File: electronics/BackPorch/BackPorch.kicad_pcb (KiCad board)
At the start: 2 copper layers, 58.7 x 41.7 mm, 15 parts, among them J1 RJ45, J2 RJ45, J3 2601-1102, J4 2601-1104, J5 2601-1104, J6 2601-1104

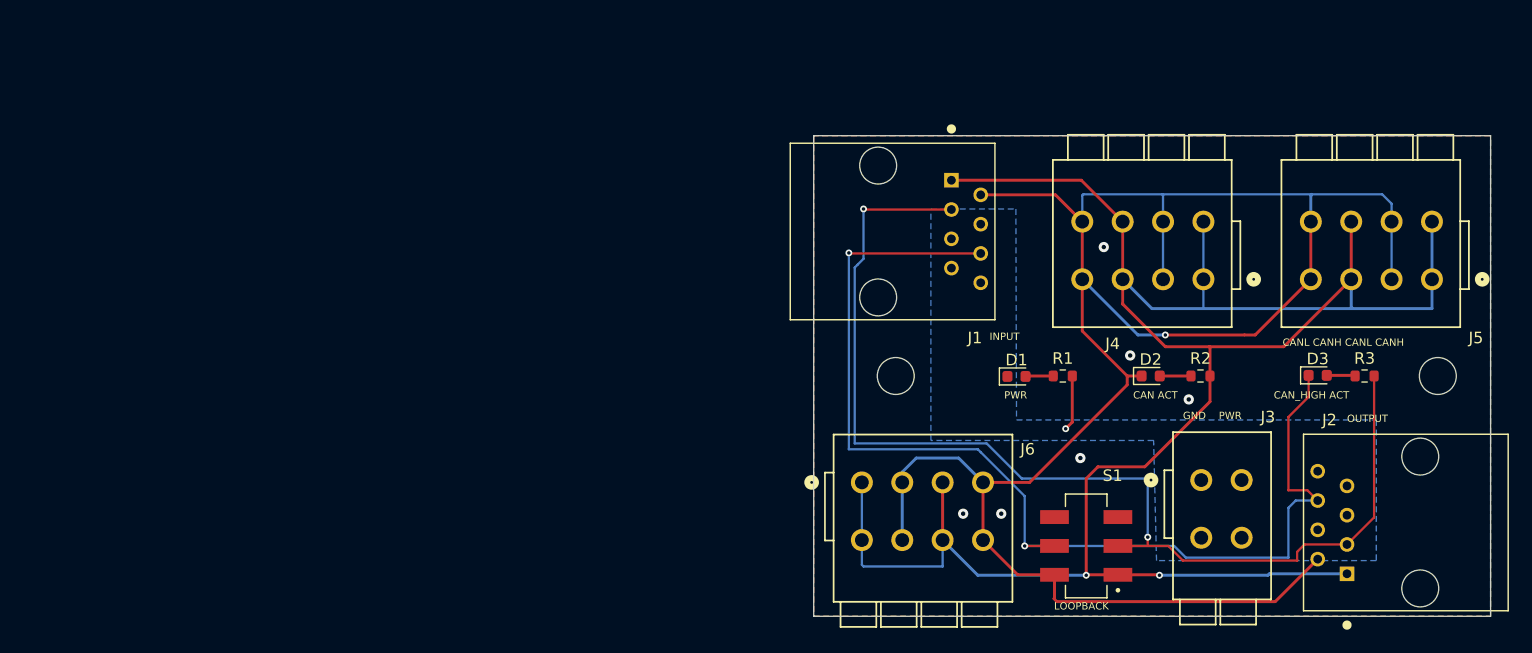
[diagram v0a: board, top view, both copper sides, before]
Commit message: Pulling Rev B into main (#1)
* Planning on ordering more back porches.
* Various updates to the footprints. Added datasheets.
* Added the software.
* Verified CAN, voltage input, current reading although the resistor is off, and temperature reading.
* Many updates to get things dialed in. Have the ABS signal working. But there is a small glitch to it.
* Inc encoder is now working as well.
* Added a bootloader.

* Bootloader is working to the point it can push new images into app code space.

* Refactored the CAN messages. Programming is working, at least pushing code. Build version strings are working correctly.

* Refactored the CAN messages. Programming is working, at least pushing code. Build version strings are working correctly.

* Bootblock will reboot on watchdog and stay in the bootblock.

* Forgot to add the auto increment version.

* Updated the bootblock functionality. I am able to program an app code image now.

* I can now reprogram app code from app code.

* Bootloading is working well.

* Updated the README file. It still needs some work.

* The bootblock now allows me to reprogram the bootblock.

* Many refactors to support different deviceIDs. Currently app code can't write to FLASH.

* This is mostly working.

* Things are working well. I can reprogram different units. The CAN status LED flashes as heartbeat messages come in.

* In the app added CAN bus utilization, sorted by device ID. Changed to the release build for the backporch, changed task names, moved can TX tasks into one thread and CAN Rx tasks into a second thread. Fixed a bug with the bootloader picking up the wrong device ID.

* Added the wpilib code. I have only tested the Java code and it works.
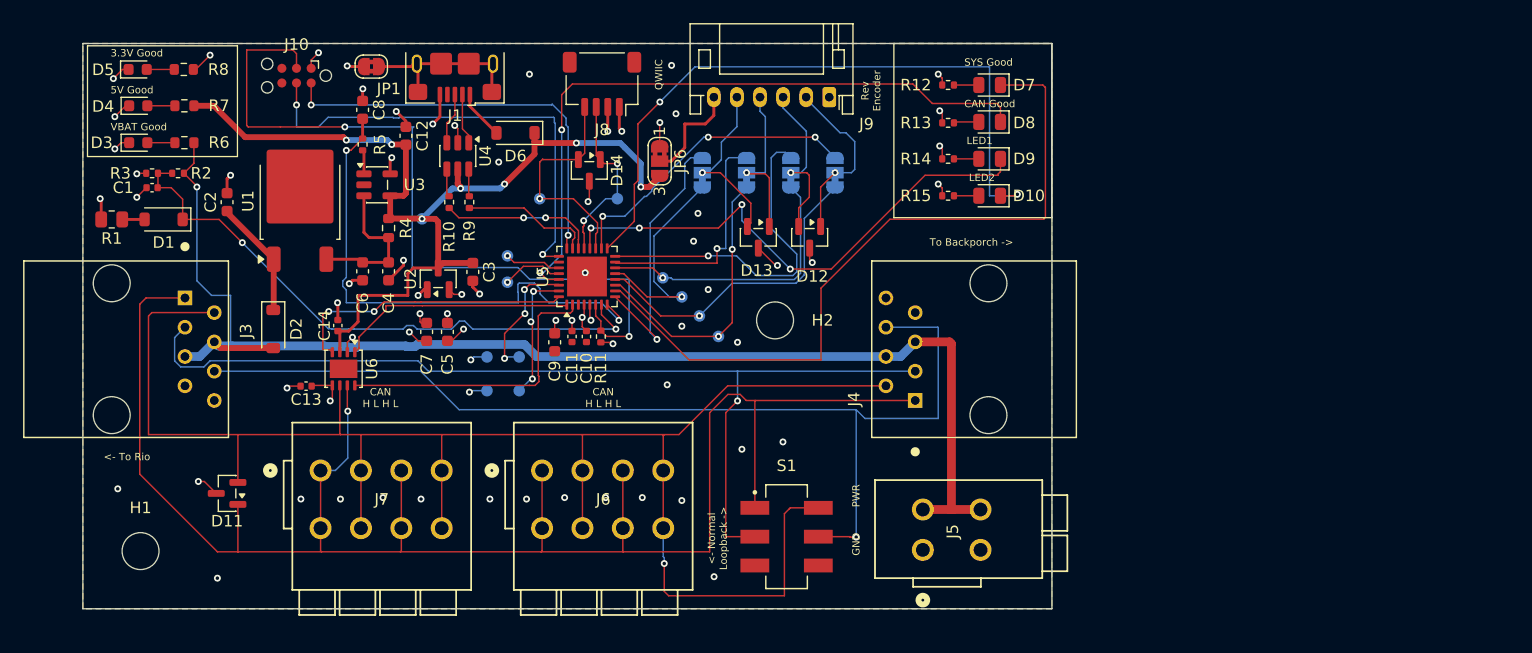
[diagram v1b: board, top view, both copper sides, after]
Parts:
- removed J2: RJ45, LocalFootprints:AMPHENOL_54602-908LF
- added C1: 1u, Capacitor_SMD:C_0402_1005Metric, F.Cu at (76.0, 83.5)
- added C10: 0.1u, Capacitor_SMD:C_0402_1005Metric, F.Cu at (113.7, 96.4)
- added C11: 0.1u, Capacitor_SMD:C_0402_1005Metric, F.Cu at (112.4, 96.4)
- added C12: 2.2u, Capacitor_SMD:C_0603_1608Metric, F.Cu at (98.0, 79.0)
- added C13: 0.1u, Capacitor_SMD:C_0402_1005Metric, F.Cu at (89.3, 100.7)
- added C14: 0.1u, Capacitor_SMD:C_0402_1005Metric, F.Cu at (92.1, 95.5)
- added C2: 10u, Capacitor_SMD:C_0603_1608Metric, F.Cu at (82.5, 84.8)
- added C3: 4.7u, Capacitor_SMD:C_0603_1608Metric, F.Cu at (103.8, 90.8)
- added C4: 10u, Capacitor_SMD:C_0603_1608Metric, F.Cu at (96.5, 90.8)
- added C5: 4.7u, Capacitor_SMD:C_0603_1608Metric, F.Cu at (101.6, 96.0)
- added C6: 10u, Capacitor_SMD:C_0603_1608Metric, F.Cu at (94.2, 90.8)
- added C7: 4.7u, Capacitor_SMD:C_0603_1608Metric, F.Cu at (99.8, 96.0)
- added C8: 2.2u, Capacitor_SMD:C_0603_1608Metric, F.Cu at (94.2, 76.8)
- added C9: 4.7u, Capacitor_SMD:C_0603_1608Metric, F.Cu at (110.9, 96.9)
- added D10: LED, LED_SMD:LED_0805_2012Metric, F.Cu at (148.6, 84.2)
- added D11: SP0502BAHT, Package_TO_SOT_SMD:SOT-23, F.Cu at (82.5, 110.0)
- added D12: SP0502BAHT, Package_TO_SOT_SMD:SOT-23, F.Cu at (133.0, 87.8)
- added D13: SP0502BAHT, Package_TO_SOT_SMD:SOT-23, F.Cu at (128.6, 87.8)
- added D14: SP0502BAHT, Package_TO_SOT_SMD:SOT-23, F.Cu at (113.9, 82.0)
- added D4: LED, LED_SMD:LED_0603_1608Metric, F.Cu at (74.8, 76.4)
- added D5: LED, LED_SMD:LED_0603_1608Metric, F.Cu at (74.8, 73.2)
- added D6: D_Schottky, Diode_SMD:D_SOD-123, F.Cu at (107.5, 78.8)
- added D7: LED, LED_SMD:LED_0805_2012Metric, F.Cu at (148.6, 74.6)
- added D8: LED, LED_SMD:LED_0805_2012Metric, F.Cu at (148.6, 77.8)
- added D9: LED, LED_SMD:LED_0805_2012Metric, F.Cu at (148.6, 81.0)
- added J10: Conn_ARM_SWD_TagConnect_TC2030-NL, Connector:Tag-Connect_TC2030-IDC-NL_2x03_P1.27mm_Vertical, F.Cu at (88.5, 73.8)
- added J7: 2601-1104, LocalFootprints:CONN4_2601-1104_WAG, F.Cu at (90.6, 108.0)
- added J8: Conn_01x04, Connector_JST:JST_SH_SM04B-SRSS-TB_1x04-1MP_P1.00mm_Horizontal, F.Cu at (115.0, 74.5)
- added J9: Conn_01x06, Connector_JST:JST_PH_S6B-PH-K_1x06_P2.00mm_Horizontal, F.Cu at (134.7, 75.7)
- added JP1: SolderJumper_2_Bridged, Jumper:SolderJumper-2_P1.3mm_Bridged2Bar_RoundedPad1.0x1.5mm, F.Cu at (95.0, 73.0)
- added JP2: SolderJumper_3_Bridged12, Jumper:SolderJumper-3_P1.3mm_Bridged12_RoundedPad1.0x1.5mm, B.Cu at (135.2, 82.2)
- added JP3: SolderJumper_3_Bridged12, Jumper:SolderJumper-3_P1.3mm_Bridged12_RoundedPad1.0x1.5mm, B.Cu at (131.4, 82.2)
- added JP4: SolderJumper_3_Bridged12, Jumper:SolderJumper-3_P1.3mm_Bridged12_RoundedPad1.0x1.5mm, B.Cu at (127.5, 82.2)
- added JP5: SolderJumper_3_Bridged12, Jumper:SolderJumper-3_P1.3mm_Bridged12_RoundedPad1.0x1.5mm, B.Cu at (123.7, 82.2)
- added JP6: SolderJumper_3_Bridged12, Jumper:SolderJumper-3_P1.3mm_Bridged2Bar12_RoundedPad1.0x1.5mm_NumberLabels, F.Cu at (120.0, 81.2)
- added R10: 22, Resistor_SMD:R_0402_1005Metric, F.Cu at (101.8, 84.8)
- added R11: 4.7k, Resistor_SMD:R_0402_1005Metric, F.Cu at (114.9, 96.4)
- added R12: 49.9, Resistor_SMD:R_0402_1005Metric, F.Cu at (145.0, 74.6)
- added R13: 49.9, Resistor_SMD:R_0402_1005Metric, F.Cu at (145.0, 77.9)
- added R14: 49.9, Resistor_SMD:R_0402_1005Metric, F.Cu at (145.0, 81.0)
- added R15: 49.9, Resistor_SMD:R_0402_1005Metric, F.Cu at (145.0, 84.2)
- added R4: 1, Resistor_SMD:R_0603_1608Metric, F.Cu at (96.5, 87.0)
- added R5: 1k, Resistor_SMD:R_0402_1005Metric, F.Cu at (94.2, 79.8)
- added R6: 680, Resistor_SMD:R_0603_1608Metric, F.Cu at (78.8, 79.6)
- added R7: 330, Resistor_SMD:R_0603_1608Metric, F.Cu at (78.8, 76.4)
- added R8: 330, Resistor_SMD:R_0603_1608Metric, F.Cu at (78.8, 73.2)
- added R9: 22, Resistor_SMD:R_0402_1005Metric, F.Cu at (103.5, 84.8)
- added TP1: TestPoint, TestPoint:TestPoint_Pad_D1.0mm, B.Cu at (105.0, 101.1)
- added TP10: TestPoint, TestPoint:TestPoint_Pad_D1.0mm, B.Cu at (121.9, 93.0)
- added TP11: TestPoint, TestPoint:TestPoint_Pad_D1.0mm, B.Cu at (123.4, 94.6)
- added TP12: TestPoint, TestPoint:TestPoint_Pad_D1.0mm, B.Cu at (106.8, 89.4)
- added TP13: TestPoint, TestPoint:TestPoint_Pad_D1.0mm, B.Cu at (106.8, 91.7)
- added TP2: TestPoint, TestPoint:TestPoint_Pad_D1.0mm, B.Cu at (99.4, 86.2)
- added TP3: TestPoint, TestPoint:TestPoint_Pad_D1.0mm, B.Cu at (105.0, 98.2)
- added TP4: TestPoint, TestPoint:TestPoint_Pad_D1.0mm, B.Cu at (107.8, 101.1)
- added TP5: TestPoint, TestPoint:TestPoint_Pad_D1.0mm, B.Cu at (107.8, 98.2)
- added TP6: TestPoint, TestPoint:TestPoint_Pad_D1.0mm, B.Cu at (109.6, 84.5)
- added TP7: TestPoint, TestPoint:TestPoint_Pad_D1.0mm, B.Cu at (116.3, 84.5)
- added TP8: TestPoint, TestPoint:TestPoint_Pad_D1.0mm, B.Cu at (125.1, 96.4)
- added TP9: TestPoint, TestPoint:TestPoint_Pad_D1.0mm, B.Cu at (120.3, 91.3)
- added U1: L78M05ABDT-TR, Package_TO_SOT_SMD:TO-252-2, F.Cu at (88.8, 84.7)
- added U2: XC6206P332MR-G, Package_TO_SOT_SMD:SOT-23, F.Cu at (100.8, 91.4)
- added U3: INA180A1, Package_TO_SOT_SMD:SOT-23-5, F.Cu at (95.5, 83.2)
- added U4: USBLC6-2SC6, Package_TO_SOT_SMD:SOT-23-6, F.Cu at (102.5, 80.8)
- added U5: STM32G0B1KBUx, Package_DFN_QFN:QFN-32-1EP_5x5mm_P0.5mm_EP3.45x3.45mm, F.Cu at (113.7, 91.2)
- added U6: TCAN1044A-Q1, Package_SON:VSON-8-1EP_3x3mm_P0.65mm_EP1.6x2.4mm, F.Cu at (92.6, 99.2)
- D1: value LED -> D_Zener; footprint LED_SMD:LED_0603_1608Metric -> Diode_SMD:D_SOD-123
- D2: value LED -> D_Schottky; footprint LED_SMD:LED_0603_1608Metric -> Diode_SMD:D_SOD-123
- H1, H2: footprint MountingHole:MountingHole_3.2mm_M3 -> MountingHole:MountingHole_3.2mm_M3_DIN965
- J1: value RJ45 -> USB_B_Micro; footprint LocalFootprints:AMPHENOL_54602-908LF -> Connector_USB:USB_Micro-B_Amphenol_10118193-0001LF_Horizontal
- J3: value 2601-1102 -> RJ45; footprint LocalFootprints:CONN2_2601-1102_WAG -> LocalFootprints:AMPHENOL_54602-908LF
- J4: value 2601-1104 -> RJ45; footprint LocalFootprints:CONN4_2601-1104_WAG -> LocalFootprints:AMPHENOL_54602-908LF
- J5: value 2601-1104 -> 2601-1102; footprint LocalFootprints:CONN4_2601-1104_WAG -> LocalFootprints:CONN2_2601-1102_WAG
- R1: value 680 -> 49.9; footprint Resistor_SMD:R_0603_1608Metric -> Resistor_SMD:R_0805_2012Metric
- R2: value 680 -> 10k; footprint Resistor_SMD:R_0603_1608Metric -> Resistor_SMD:R_0402_1005Metric
- R3: value 680 -> 1k; footprint Resistor_SMD:R_0603_1608Metric -> Resistor_SMD:R_0402_1005Metric
- moved R3 106.6 mm to (76.0, 82.2)
- moved D3 104.2 mm to (74.8, 79.6)
- moved J3 95.1 mm to (72.5, 97.5), turned to -90 degrees
- moved R2 90.4 mm to (78.2, 82.2)
- moved R1 83.5 mm to (72.5, 86.2)
- moved D2 76.2 mm to (86.5, 95.8), turned to -90 degrees
- moved D1 75.2 mm to (77.0, 86.2), turned to 180 degrees
- moved H1 67.2 mm to (75.0, 115.0)
- moved H2 57.7 mm to (130.0, 95.0)
- moved J5 50.0 mm to (142.8, 114.9), turned to 90 degrees
- moved J1 39.5 mm to (102.2, 72.8), turned to 180 degrees
- moved J6 27.7 mm to (109.8, 108.0)
- moved S1 26.0 mm to (131.0, 113.8), turned to -90 degrees
- moved J4 19.6 mm to (148.5, 97.5), turned to 90 degrees
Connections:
- D1 pad 1: GND -> VIN_MEAS
- D2 pad 1: /CAN_LOW -> Net-(D2-K)
- D2 pad 2: Net-(D2-A) -> VIN
- D3 pad 1: /CAN_LOW_LOOP -> GND
- J1 pad 1: /CAN_HIGH -> Net-(D6-A)
- J1 pad 2: /CAN_LOW -> Net-(J1-D-)
- J1 pad 3: /CAN_HIGH_LOOP -> Net-(J1-D+)
- J1 pad 4: /VBAT -> unconnected-(J1-ID-Pad4)
- J1 pad 5: /VBAT -> GND
- J1 pad 6: /CAN_LOW_LOOP -> Net-(J1-Shield)
- J3 pad 1: GND -> /IO/CAN_HIGH
- J3 pad 2: GND -> /IO/CAN_LOW
- J3 pad 3: /VBAT -> /IO/CAN_HIGH_LOOP
- J3 pad 4: /VBAT -> VIN
- J4 pad 1: /CAN_HIGH -> /IO/CAN_HIGH
- J4 pad 2: /CAN_HIGH -> /IO/CAN_LOW
- J4 pad 3: /CAN_LOW -> /IO/CAN_HIGH_LOOP
- J4 pad 4: /CAN_LOW -> VIN
- J4 pad 5: /CAN_HIGH -> VIN
- J4 pad 6: /CAN_HIGH -> /IO/CAN_LOW_LOOP
- J4 pad 7: /CAN_LOW -> GND
- J4 pad 8: /CAN_LOW -> GND
- J5 pad 1: /CAN_HIGH -> GND
- J5 pad 2: /CAN_HIGH -> GND
- J5 pad 3: /CAN_LOW -> VIN
- J5 pad 4: /CAN_LOW -> VIN
- J6 pad 1: /CAN_HIGH -> /IO/CAN_HIGH
- J6 pad 2: /CAN_HIGH -> /IO/CAN_HIGH
- J6 pad 3: /CAN_LOW -> /IO/CAN_LOW
- J6 pad 4: /CAN_LOW -> /IO/CAN_LOW
- J6 pad 5: /CAN_HIGH -> /IO/CAN_HIGH
- J6 pad 6: /CAN_HIGH -> /IO/CAN_HIGH
- J6 pad 7: /CAN_LOW -> /IO/CAN_LOW
- J6 pad 8: /CAN_LOW -> /IO/CAN_LOW
- R1 pad 1: /VBAT -> Net-(D1-A)
- R1 pad 2: Net-(D1-A) -> GND
- R2 pad 1: /CAN_HIGH -> VIN
- R2 pad 2: Net-(D2-A) -> VIN_MEAS
- R3 pad 1: /CAN_HIGH_LOOP -> VIN_MEAS
- R3 pad 2: Net-(D3-A) -> GND
- S1 pad 1: /CAN_HIGH -> /IO/CAN_HIGH
- S1 pad 2: /CAN_HIGH_LOOP -> /IO/CAN_HIGH_LOOP
- S1 pad 4: /CAN_LOW -> /IO/CAN_LOW
- S1 pad 5: /CAN_LOW_LOOP -> /IO/CAN_LOW_LOOP
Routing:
- net /CAN_HIGH: track 182.3 -> 0.00 mm, vias 2 -> 0
- net /CAN_LOW: track 170.7 -> 0.00 mm, vias 1 -> 0
- net /IO/CAN_HIGH: track 0.00 -> 152.7 mm, vias 0 -> 1
- net /IO/CAN_LOW: track 0.00 -> 149.1 mm, vias 0 -> 1
- net VIN: track 0.00 -> 113.7 mm, vias 0 -> 1
- net /CAN_HIGH_LOOP: track 97.8 -> 0.00 mm, vias 2 -> 0
- net /CAN_LOW_LOOP: track 96.3 -> 0.00 mm, vias 2 -> 0
- net /IO/CAN_LOW_LOOP: track 0.00 -> 91.2 mm, vias 0 -> 1
- net /IO/CAN_HIGH_LOOP: track 0.00 -> 85.6 mm, vias 0 -> 1
- net VCC: track 0.00 -> 84.2 mm, vias 0 -> 7
- net NRST: track 0.00 -> 68.3 mm, vias 0 -> 2
- net SYS_STATUS: track 0.00 -> 63.8 mm
- net LED2: track 0.00 -> 59.6 mm, vias 0 -> 2
- net CAN_STATUS: track 0.00 -> 58.8 mm, vias 0 -> 2
- net VIN_MEAS: track 0.00 -> 51.8 mm, vias 0 -> 2
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- added copper zone on In2.Cu, net 3V3
- added copper zone on In1.Cu, net GND
- removed copper zone on B.Cu, net /VBAT
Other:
- board size 58.7 x 41.7 mm -> 84 x 49 mm
- copper layers 2 -> 4
- board text added: "3.3V Good"
- board text added: "5V Good"
- board text added: "<- Normal Loopback ->"
- board text added: "<- To Rio"
- board text added: "Backporch Rev B Team 4360 and 7048"
- board text added: "CAN Good"
- board text added: "CAN H L H L"
- board text added: "GND"
- board text added: "LED1"
- board text added: "LED2"
- board text added: "QWIIC"
- board text added: "Rev Encoder"
- board text added: "SYS Good"
- board text added: "TP1 = 3.3V TP2 = 5V TP3 = GND TP4 = SPARE2 TP5 = SPARE1 TP6 = SCL TP7 = SDA TP8 = CS TP9 = MOSI TP10 = MISO TP11 = CLK TP12 = TX TP13 = RX"
- board text added: "To Backporch ->"
- board text added: "VBAT Good"
- board text removed: "CAN ACT"
- board text removed: "CANL CANH CANL CANH"
- board text removed: "CAN_HIGH ACT"
- board text removed: "GND PWR"
- board text removed: "INPUT"
- board text removed: "LOOPBACK"
- board text removed: "OUTPUT"
